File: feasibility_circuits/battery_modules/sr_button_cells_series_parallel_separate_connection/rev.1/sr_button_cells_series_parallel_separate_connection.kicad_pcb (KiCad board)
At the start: 2 copper layers, 86.4 x 68.6 mm, 25 parts, among them J1 Batt Out, J10 CONN_01X01, J11 CONN_01X01, J12 CONN_01X01, J13 CONN_01X01, J14 CONN_01X01, J15 Parallel, J16 Series, J17 Cell2, J18 Cell1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

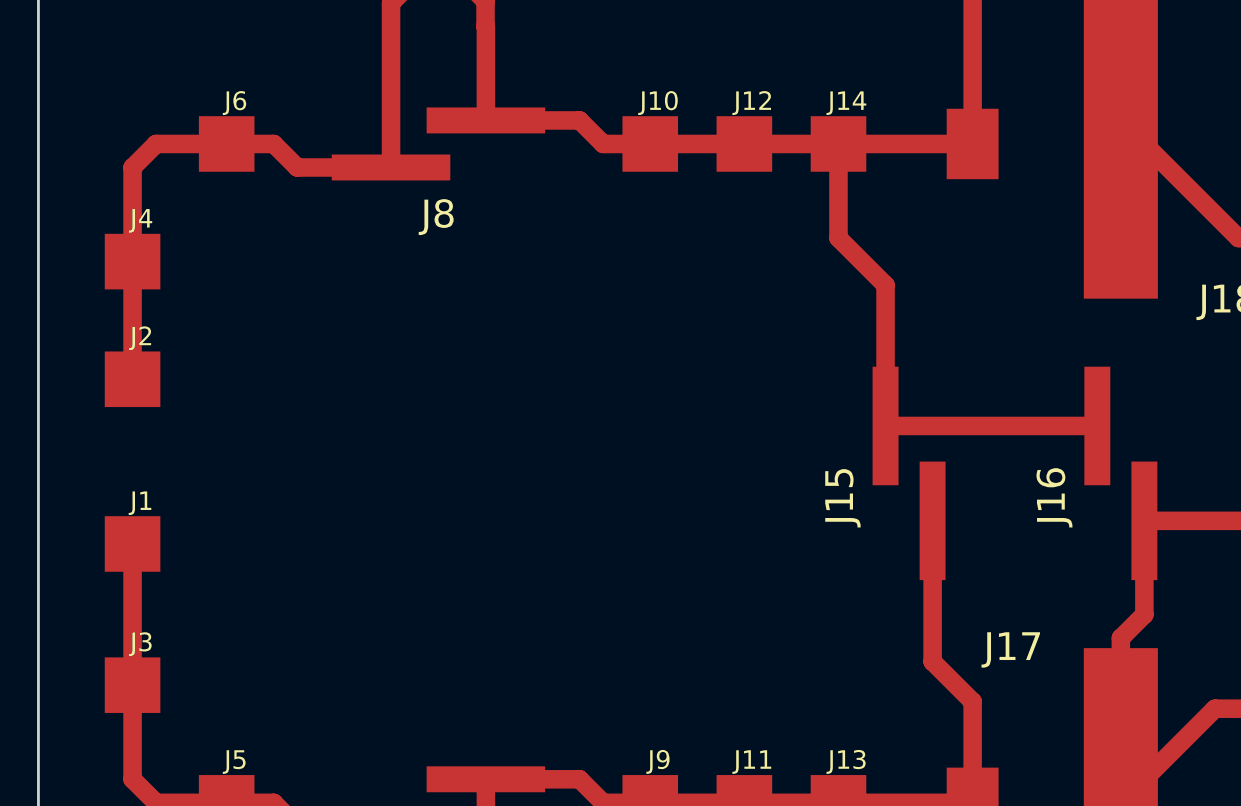
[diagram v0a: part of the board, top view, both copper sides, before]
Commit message: Added holder for Lithium-Ion cell to battery board
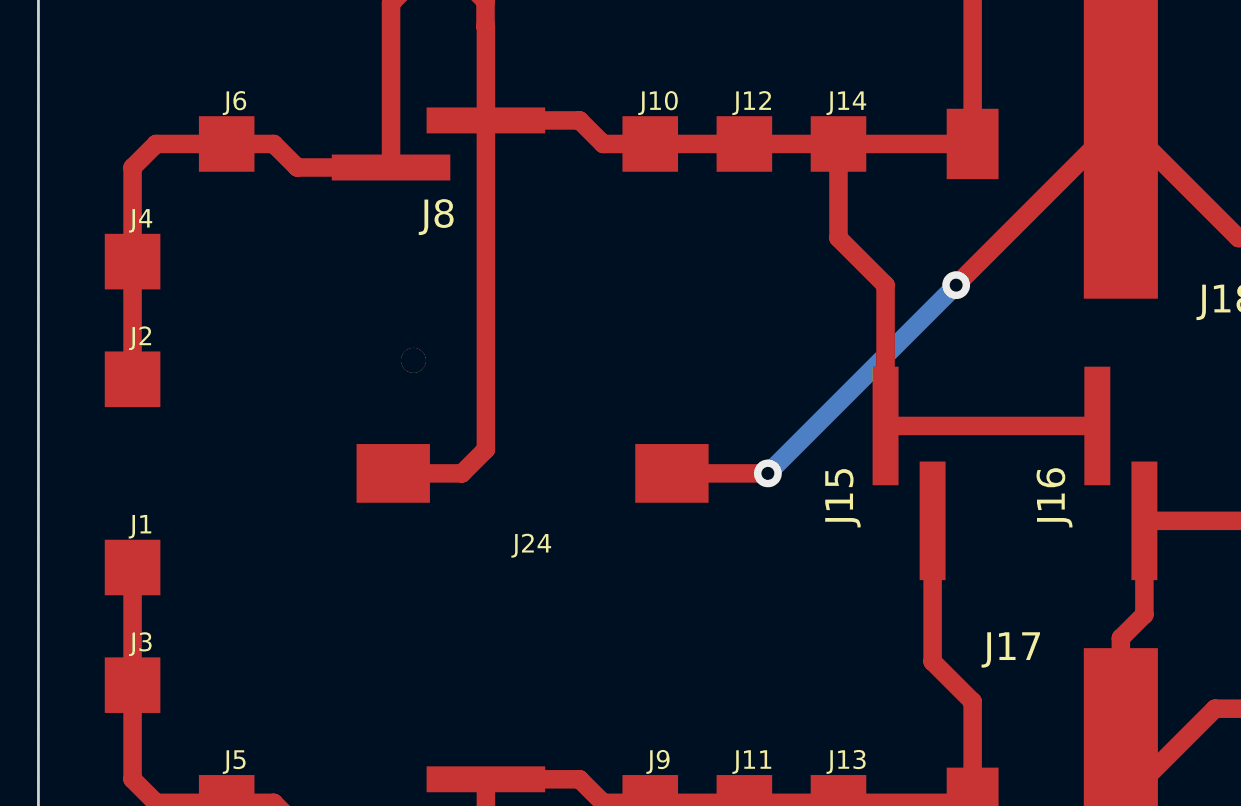
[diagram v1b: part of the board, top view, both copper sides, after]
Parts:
- added J24: Lithium-Ion Cell, Custom Battery Products:proto_button_cell_holder-smd-498, F.Cu at (147.3, 96.5)
- moved J1 1.27 mm to (125.7, 101.6)
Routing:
- net Net-(J18-Pad3): track 40.2 -> 71.8 mm, vias 0 -> 2
- net Net-(J10-Pad1): track 98.1 -> 121.4 mm
- net Net-(J1-Pad1): track 35.8 -> 34.6 mm
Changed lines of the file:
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@@
 (kicad_pcb (version 4) (host pcbnew 4.0.4-stable)
   (general
-    (links 30)
+    (links 32)
     (no_connects 0)
-    (area 123.213334 66.38 203.376666 127.93)
+    (area 120.574999 62.154999 207.085001 130.885001)
     (thickness 1.6)
     (drawings 8)
-    (tracks 72)
+    (tracks 81)
     (zones 0)
-    (modules 25)
+    (modules 26)
     (nets 7)
   )
@@
   (layers
     (0 F.Cu signal)
-    (31 B.Cu signal)
+    (31 B.Cu signal hide)
     (32 B.Adhes user)
     (33 F.Adhes user)
@@
   )
   (module "Custom Connectors:proto_pad-square-3mm" (layer F.Cu)
-    (at 125.73 100.33)
+    (at 125.73 101.6)
     (descr "3 mm square SMD Pad e.g. for soldering wires ")
     (tags CONN)
@@
     )
   )
+  (module "Custom Battery Products:proto_button_cell_holder-smd-498" (layer F.Cu)
+    (at 147.32 96.52)
+    (fp_text reference J24 (at 0 3.81) (layer F.SilkS)
+      (effects (font (size 1 1) (thickness 0.15)))
+    )
+    (fp_text value "Lithium-Ion Cell" (at 0 -9.1) (layer F.Fab)
+      (effects (font (size 1 1) (thickness 0.15)))
+    )
+    (pad 2 smd rect (at 7.52 0) (size 3.96 3.17) (layers F.Cu F.Paste F.Mask)
+      (net 6 "Net-(J18-Pad3)"))
+    (pad "" thru_hole circle (at -6.43 -6.1) (size 1.35 1.35) (drill 1.35) (layers *.Cu *.Mask))
+    (pad 1 smd rect (at -7.52 0) (size 3.96 3.17) (layers F.Cu F.Paste F.Mask)
+      (net 4 "Net-(J10-Pad1)"))
+  )
   (gr_line (start 207.01 130.81) (end 179.07 130.81) (angle 90) (layer Edge.Cuts) (width 0.15))
   (gr_line (start 207.01 62.23) (end 207.01 130.81) (angle 90) (layer Edge.Cuts) (width 0.15))
@@
   (gr_line (start 120.65 130.81) (end 120.65 62.23) (angle 90) (layer Edge.Cuts) (width 0.15))
   (gr_line (start 179.07 130.81) (end 120.65 130.81) (angle 90) (layer Edge.Cuts) (width 0.15))
+  (segment (start 125.73 107.95) (end 125.73 101.6) (width 1) (layer F.Cu) (net 1))
   (segment (start 140.89 123.19) (end 140.89 123.11) (width 1) (layer F.Cu) (net 1))
   (segment (start 140.89 123.11) (end 139.68 121.9) (width 1) (layer F.Cu) (net 1))
@@
   (segment (start 134.62 115.57) (end 139.68 115.57) (width 1) (layer F.Cu) (net 1))
   (segment (start 133.35 114.3) (end 134.62 115.57) (width 1) (layer F.Cu) (net 1))
-  (segment (start 125.73 100.33) (end 125.73 107.95) (width 1) (layer F.Cu) (net 1))
   (segment (start 125.73 107.95) (end 125.73 113.03) (width 1) (layer F.Cu) (net 1))
   (segment (start 125.73 113.03) (end 127 114.3) (width 1) (layer F.Cu) (net 1))
@@
   (segment (start 151.13 114.3) (end 153.67 114.3) (width 1) (layer F.Cu) (net 3))
   (segment (start 149.86 113.03) (end 151.13 114.3) (width 1) (layer F.Cu) (net 3))
+  (segment (start 139.8 96.52) (end 143.51 96.52) (width 1) (layer F.Cu) (net 4) (status 400000))
+  (segment (start 144.8 95.23) (end 144.8 77.47) (width 1) (layer F.Cu) (net 4) (status 800000))
+  (segment (start 143.51 96.52) (end 144.8 95.23) (width 1) (layer F.Cu) (net 4))
   (segment (start 144.8 77.47) (end 144.8 72.41) (width 1) (layer F.Cu) (net 4))
   (segment (start 144.78 71.04) (end 143.59 69.85) (width 1) (layer F.Cu) (net 4))
@@
   (segment (start 194.31 109.22) (end 200.66 109.22) (width 1) (layer F.Cu) (net 5))
   (segment (start 180.34 99.08) (end 191.77 99.08) (width 1) (layer F.Cu) (net 5))
+  (segment (start 154.84 96.52) (end 160.02 96.52) (width 1) (layer F.Cu) (net 6) (status 400000))
+  (segment (start 170.18 86.36) (end 177.8 78.74) (width 1) (layer F.Cu) (net 6) (status 800000))
+  (via (at 170.18 86.36) (size 1.5) (drill 0.7) (layers F.Cu B.Cu) (net 6))
+  (segment (start 160.02 96.52) (end 170.18 86.36) (width 1) (layer B.Cu) (net 6))
+  (via (at 160.02 96.52) (size 1.5) (drill 0.7) (layers F.Cu B.Cu) (net 6))
+  (segment (start 177.8 78.74) (end 179.07 78.74) (width 1) (layer F.Cu) (net 6) (status C00000))
   (segment (start 189.23 93.96) (end 189.23 83.82) (width 1) (layer F.Cu) (net 6))
   (segment (start 194.31 78.74) (end 194.31 83.82) (width 1) (layer F.Cu) (net 6))
